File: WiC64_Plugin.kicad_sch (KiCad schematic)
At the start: 60 parts, among them CN1 USERPORT-C64, CN2 OLED0.96, Q1 BSS138, Q10 BSS138, Q11 BSS138, Q2 BSS138, Q3 BSS138, Q4 BSS138, Q5 BSS138, Q6 BSS138, Q7 BSS138, Q8 BSS138, Q9 BSS138, SW1 RESET-C64, SW2 Function, U1 ESP32_DevKit_V1_DOIT, U2 ESP-01

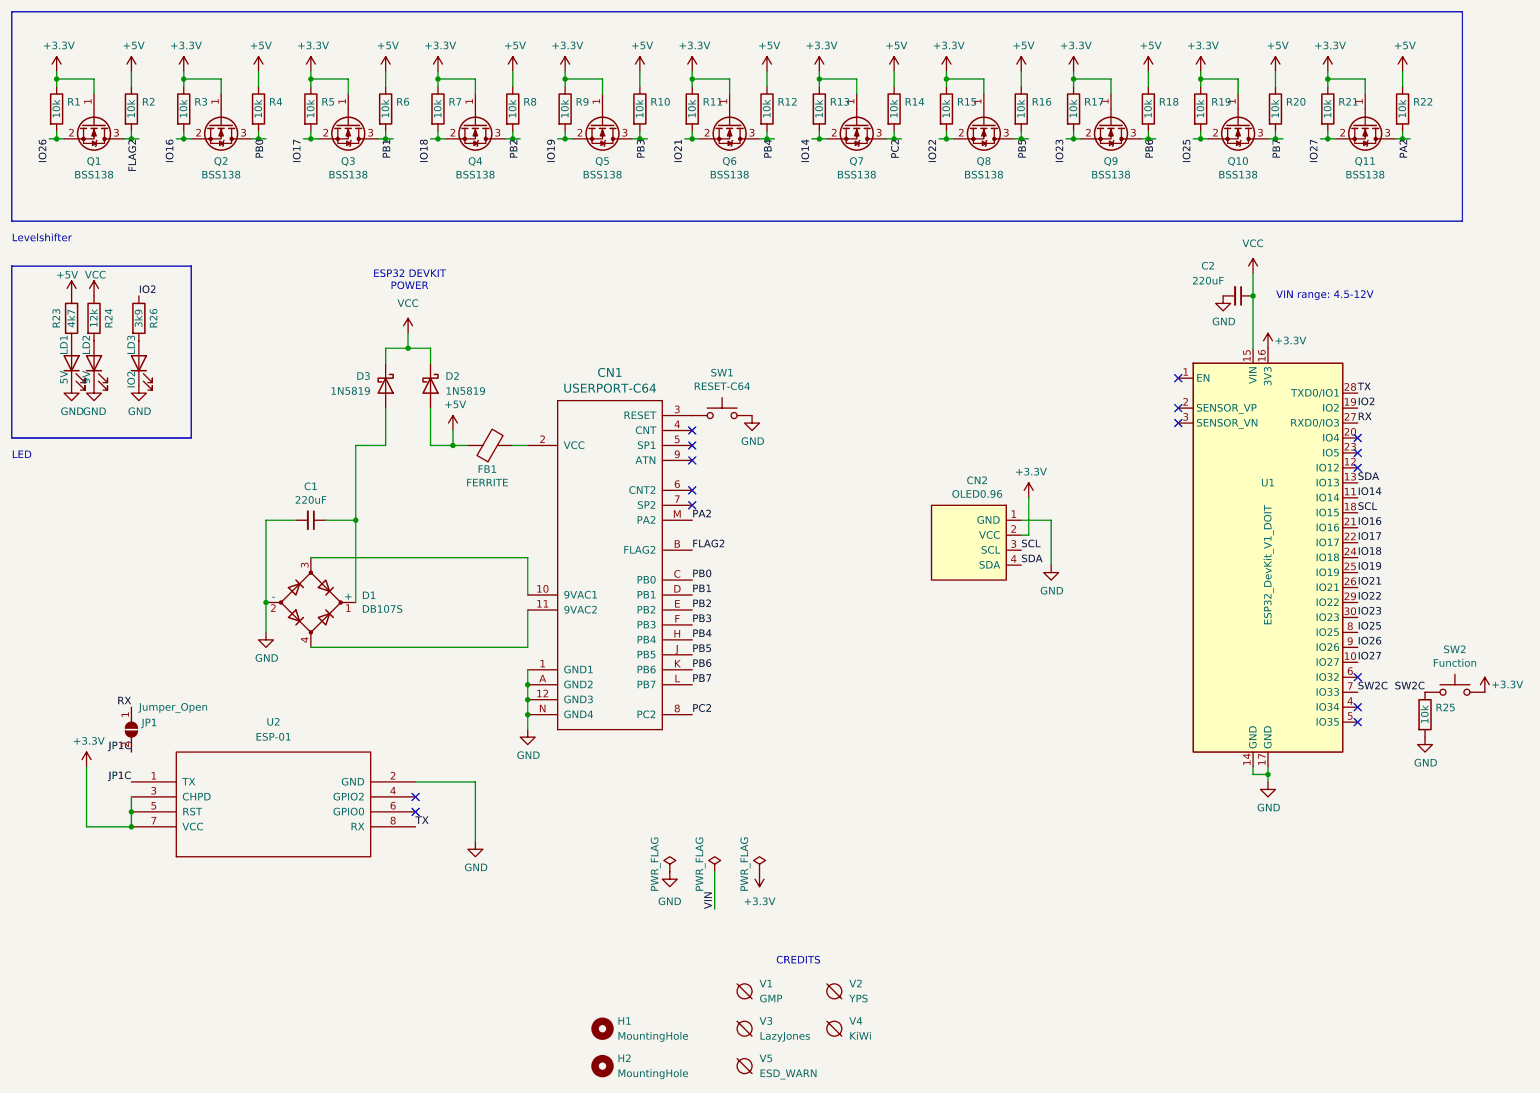
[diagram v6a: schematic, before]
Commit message: Add Pear logo + Connect 9V power led to actual 9V
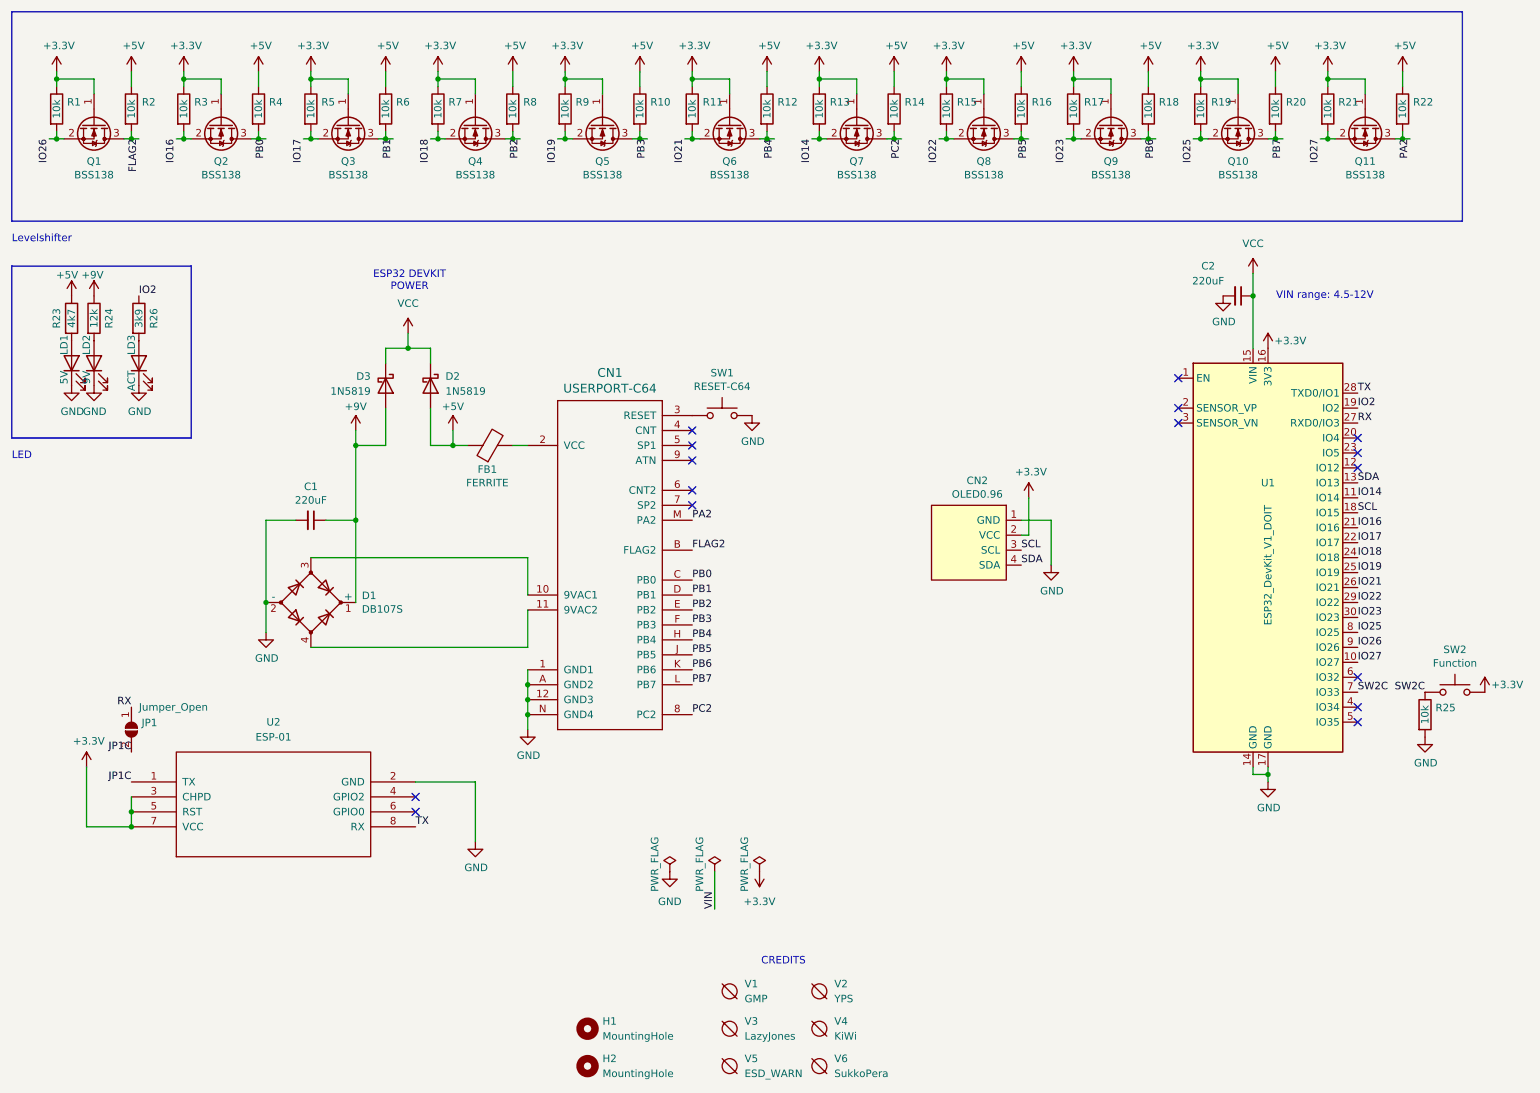
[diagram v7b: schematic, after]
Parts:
- added V6: SukkoPera, WiC64:PearLogo, symbol void:Void
- LD3: value IO2 -> ACT
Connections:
- net VCC: no longer R24.1
- net +9V: now reaches C1.1, D1.1 (+), D3.2 (A)
- net +9V: now also R24.1
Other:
- moved on the sheet: H1, H2, V1, V2, V3, V4, V5
